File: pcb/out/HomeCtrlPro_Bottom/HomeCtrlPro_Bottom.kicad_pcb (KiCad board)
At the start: 2 copper layers, 168.4 x 100.2 mm, 188 parts, among them J1 B2B, J10 OUT6, J11 OUT7, J12 OUTDC8, J13 OUTDC9, J14 OUTDC10, J15 OUTDC11, J16 OUTDC12, J17 OUTDC13, J18 OUTDC14, J19 OUTDC15, J2 24V, J3 230V, J4 OUT0, J5 OUT1, J6 OUT2, J7 OUT3, J8 OUT4, J9 OUT5, K1 SRD-24V, K2 SRD-24V, K3 SRD-24V, K4 SRD-24V, K5 SRD-24V, K6 SRD-24V, K7 SRD-24V, K8 SRD-24V, Q1 BC547, Q10 IRLZ44N, Q11 IRLZ44N, Q12 IRLZ44N, Q13 IRLZ44N, Q14 IRLZ44N, Q15 IRLZ44N, Q16 IRLZ44N, Q2 BC547, Q3 BC547, Q4 BC547, Q5 BC547, Q6 BC547, Q7 BC547, Q8 BC547, Q9 IRLZ44N, U1 MP1584, U2 AMS1117-3.3, U3 MCP23017

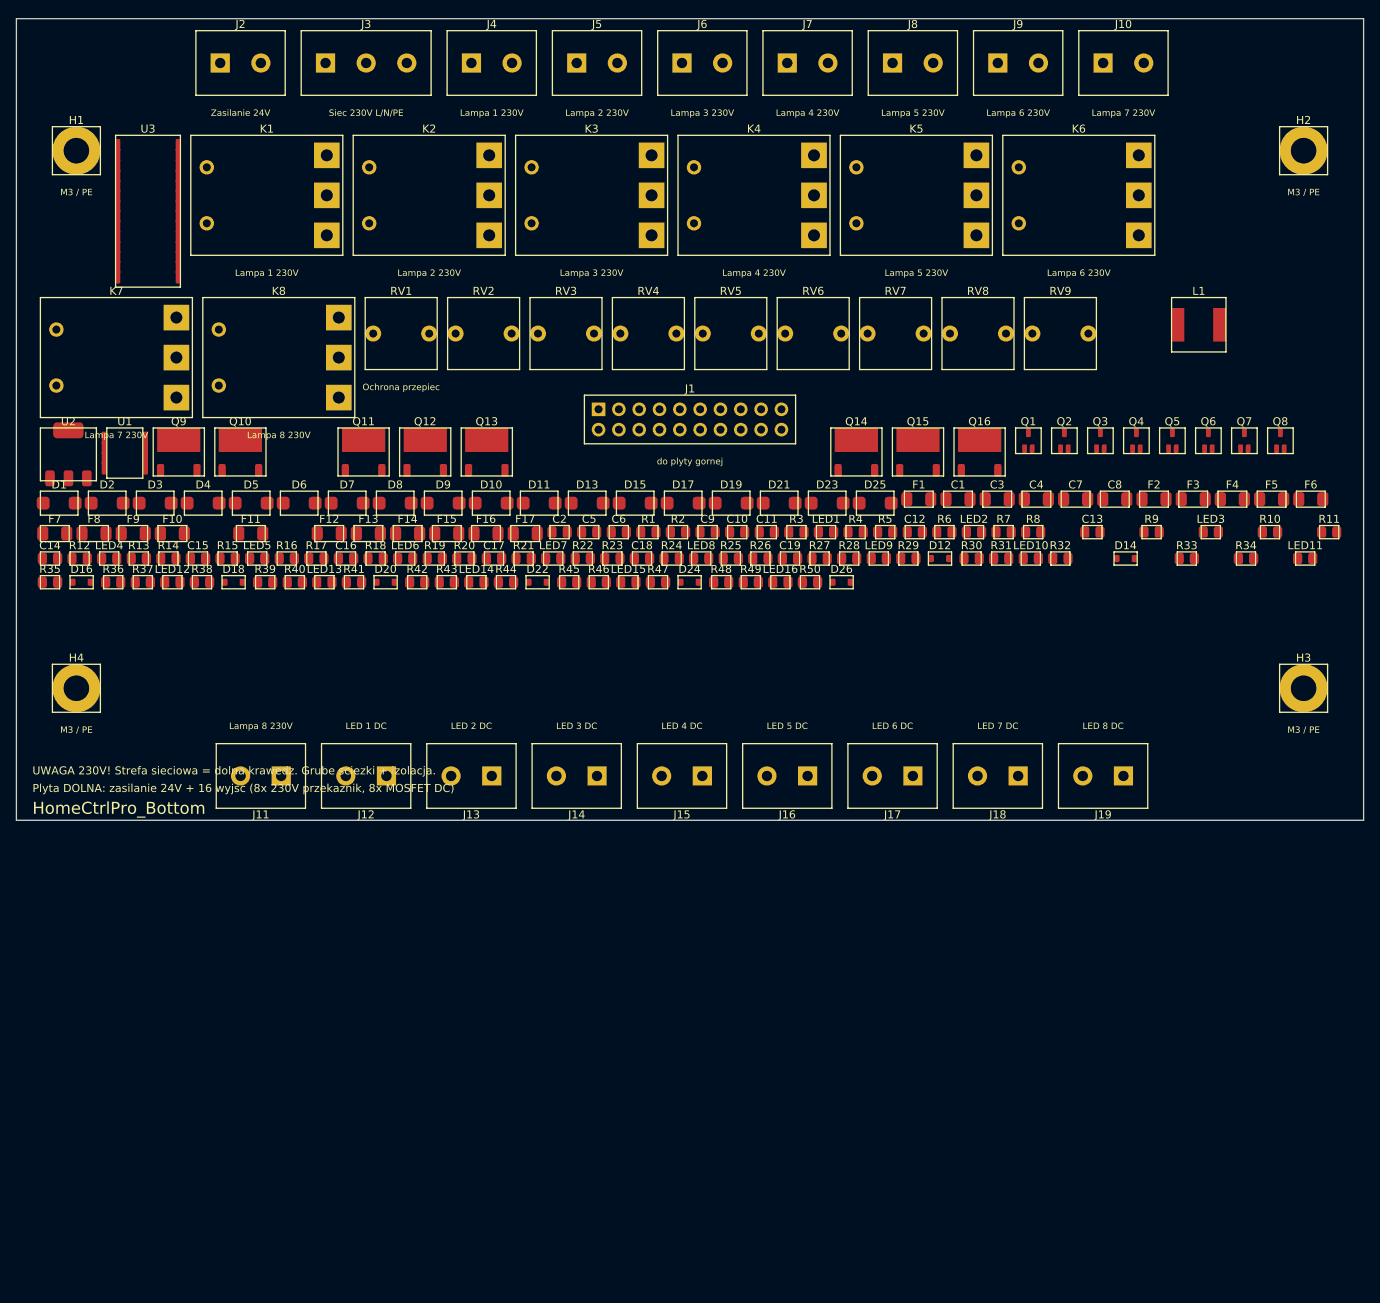
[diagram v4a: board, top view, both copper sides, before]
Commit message: Uklad na 4 krawedziach (plyta ~kwadratowa): wejscia gora+lewo, wyjscia dol+prawo
- Nowy tryb auto_layout_4e + place_board_4e: zlacza rozlozone na 4 krawedziach,
  zlacza na bokach obrocone 90/270 (_place_side), rotacjo-swiadome obrysy (_ext, DRC).
- Otwory w WEWNETRZNYCH narozach (wewnatrz pasow zlacz obu plyt) - brak kolizji
  otwor-zlacze; B2B w srodku. Wspolne wspolrzedne.
- _pack nigdy nie naklada (rosnie w dol zamiast nachodzic na przeszkody).
- Przyciski TFT przeniesione do wnetrza (przy ekranie).

HomeCtrlPro: zlacza na calym obwodzie, ~kwadrat 128x158 (z 280x185).
Oba PCB 0/0/0, testy 12/12, kiutils OK.

Co-Authored-By: Claude Opus 4.8 (1M context) <noreply@anthropic.com>
Claude-Session: https://claude.ai/code/session_01LNGxtK2Jv1rJLBLPTwFQ9C
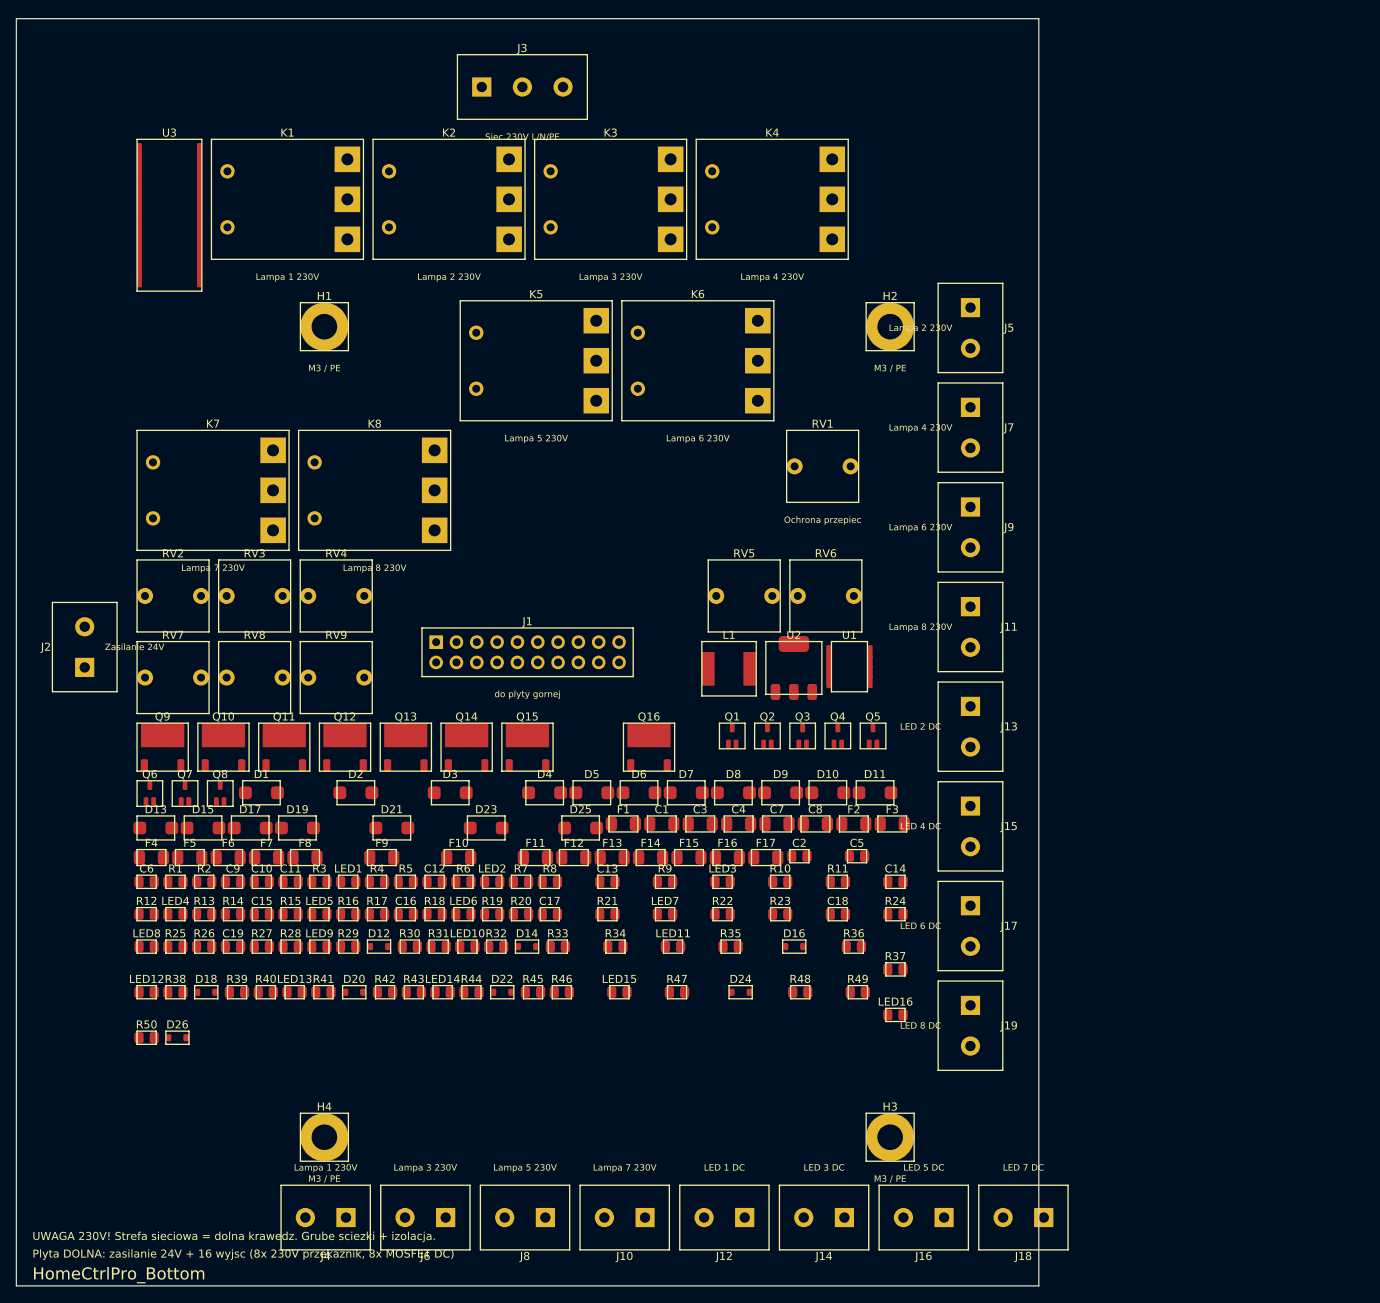
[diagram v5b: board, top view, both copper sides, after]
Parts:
- moved J10 157.2 mm to (76.0, 149.9), turned to 180 degrees
- moved J8 152.2 mm to (63.6, 149.9), turned to 180 degrees
- moved J6 148.4 mm to (51.1, 149.9), turned to 180 degrees
- moved J4 145.8 mm to (38.7, 149.9), turned to 180 degrees
- moved F6 142.5 mm to (26.5, 104.9)
- moved F5 142.4 mm to (21.7, 104.9)
- moved F4 142.4 mm to (16.9, 104.9)
- moved Q8 139.7 mm to (25.5, 96.9)
- moved Q7 139.6 mm to (21.1, 96.9)
- moved Q6 139.5 mm to (16.7, 96.9)
- moved C14 113.1 mm to (109.9, 107.9)
- moved R37 105.8 mm to (109.9, 118.8)
- moved R36 103.2 mm to (104.7, 116.0)
- moved D26 100.7 mm to (20.1, 127.4)
- moved R50 100.6 mm to (16.3, 127.4)
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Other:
- board size 168.4 x 100.2 mm -> 127.8 x 158.4 mm

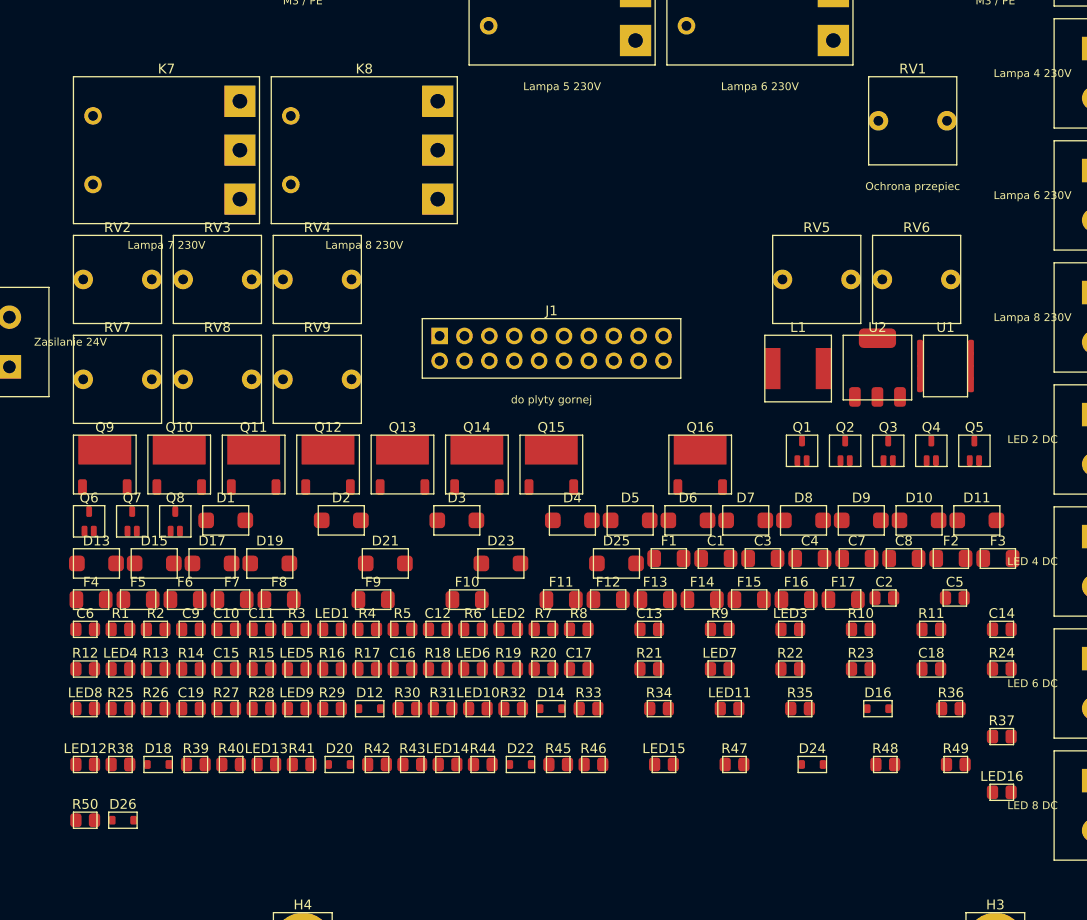
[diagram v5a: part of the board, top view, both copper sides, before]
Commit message: Uporzadkuj rozstaw R/C: grupowanie identycznych czesci w rowne rzedy
_pack sortuje po (wysokosc, szerokosc, typ, wartosc) - identyczne rezystory/
kondensatory/LED-y trafiaja obok siebie w regularnych rzedach zamiast losowego
wymieszania. Czytelniejszy, uporzadkowany uklad wnetrza. Oba PCB 0/0/0, testy 12/12.

Co-Authored-By: Claude Opus 4.8 (1M context) <noreply@anthropic.com>
Claude-Session: https://claude.ai/code/session_01LNGxtK2Jv1rJLBLPTwFQ9C
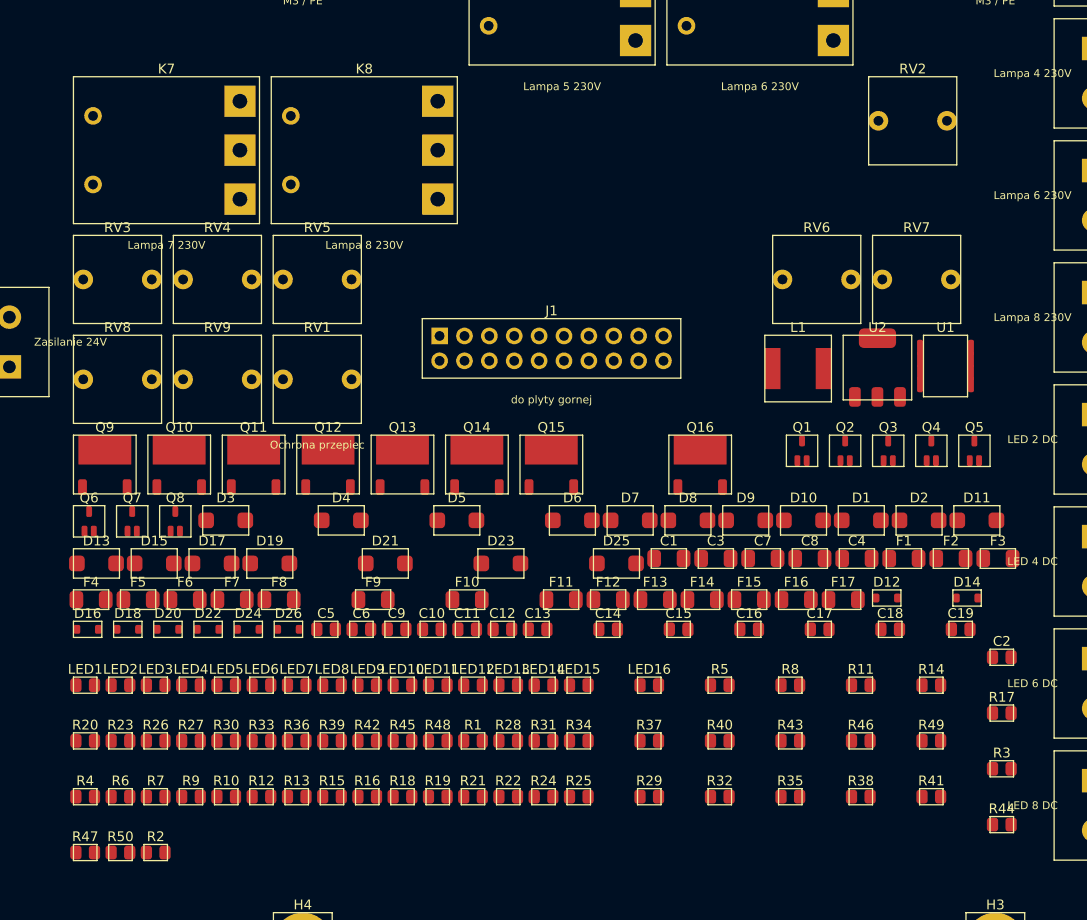
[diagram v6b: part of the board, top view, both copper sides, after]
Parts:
- moved RV2 82.8 mm to (100.8, 56.0)
- moved RV7 82.2 mm to (101.2, 72.2)
- moved D16 81.1 mm to (16.5, 107.9)
- moved C19 79.0 mm to (105.7, 107.9)
- moved R23 76.0 mm to (19.9, 119.3)
- moved R38 75.7 mm to (95.5, 125.0)
- moved R14 75.6 mm to (102.7, 113.6)
- moved R3 73.4 mm to (109.9, 122.1)
- moved R10 67.0 mm to (30.7, 125.0)
- moved R47 66.9 mm to (16.3, 130.7)
- moved R36 66.9 mm to (37.9, 119.3)
- moved RV1 66.3 mm to (40.0, 82.4)
- moved LED3 65.1 mm to (23.5, 113.6)
- moved R17 65.0 mm to (109.9, 116.4)
- moved D1 64.9 mm to (95.5, 96.8)
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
